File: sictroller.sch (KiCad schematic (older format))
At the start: 16 parts

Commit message: Hierarchical schematic
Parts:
- removed C? (x2): 1uF, symbol C_Small
- removed J?: TMDSCNCD28069, MODULE, symbol TMDSCNCD28069
- removed J?: CONN_02X13, symbol CONN_02X13
- removed J?: CONN_01X07, symbol CONN_01X07
- removed R? (x3): 10k, symbol R_Small
- removed R? (x6): 5k1, symbol R_Small
- removed R?: 10k, symbol R_ARRAY_8_10
- removed U?: 74LVC8T245, symbol 74LVC8T245
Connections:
- net labels removed: +15V, +3.3V, +5VD, FLT_DESAT, FLT_DESAT_LV, FLT_OTP, FLT_OTP_LV, GNDD, HV+, HV-, PHASE_A, PHASE_B, PHASE_C, PWM_AH, PWM_AL, PWM_BH, PWM_BL, PWM_CH, PWM_CL, PWR_RDY, PWR_RDY_LV, PWR_TEMP, ~PWR_RESET
- wire segments 103 -> 0
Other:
- note removed: "HV signals - use Micro-Fit, \nwatch creepage"

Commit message: V0 schematic complete (?)
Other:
- note added: "TODO (better):\nWelded contactor detection / protection\nLV from HV, LV batt charging?\nTemperature - motor, heatsink, power stage, air, batt?\nCrosslink to other string\nHuman interface\nContactor outputs (3 phases + bus + ?)\nADC precision reference\nCrystal oscillator\nGPS and air data interface"
- note added: "TODO (minimal):\nAux ADC and other signals on controlcard"
- note removed: "TODO (better):\nLV from HV, LV batt charging?\nTemperature - motor, heatsink, power stage, air, batt?\nCrosslink to other string\nHuman interface\nContactor outputs (3 phases + bus + ?)\nADC precision reference\nCrystal oscillator\nGPS and air data interface"
- note removed: "TODO (minimal):\n15V in, 5V and 3.3V reg\nPWM and faults to controlcard\nHV V and I monitoring inc filters\nPhase current (ext hall effect) inc filters\nPhase voltage inc filters\n(desired) bridge current via Vds inc filters"
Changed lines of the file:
@@
 LIBS:TMDSCNCD28069
 LIBS:74LVC8T245
+LIBS:MAX4195
 LIBS:sictroller-cache
 EELAYER 25 0
@@
 $EndDescr
 Text Notes 750  7900 0    60   ~ 0
-TODO (minimal):\n15V in, 5V and 3.3V reg\nPWM and faults to controlcard\nHV V and I monitoring inc filters\nPhase current (ext hall effect) inc filters\nPhase voltage inc filters\n(desired) bridge current via Vds inc filters
+TODO (minimal):\nAux ADC and other signals on controlcard
 Text Notes 3600 7900 0    60   ~ 0
-TODO (better):\nLV from HV, LV batt charging?\nTemperature - motor, heatsink, power stage, air, batt?\nCrosslink to other string\nHuman interface\nContactor outputs (3 phases + bus + ?)\nADC precision reference\nCrystal oscillator\nGPS and air data interface
+TODO (better):\nWelded contactor detection / protection\nLV from HV, LV batt charging?\nTemperature - motor, heatsink, power stage, air, batt?\nCrosslink to other string\nHuman interface\nContactor outputs (3 phases + bus + ?)\nADC precision reference\nCrystal oscillator\nGPS and air data interface
 $Sheet
-S 2650 1050 2350 3100
+S 4750 1500 2350 1850
 U 57A162B5
 F0 "Control Card" 60
 F1 "controlcard.sch" 60
+F2 "VFB_A" I L 4750 1900 60
+F3 "VFB_B" I L 4750 2000 60
+F4 "VFB_C" I L 4750 2100 60
+F5 "VFB_BUS" I L 4750 2200 60
+F6 "IFB_A" I L 4750 2350 60
+F7 "IFB_B" I L 4750 2450 60
+F8 "IFB_C" I L 4750 2550 60
+F9 "PWR_STG_TEMP" I L 4750 1650 60
+F10 "MOTOR_TEMP" I L 4750 1750 60
+F11 "IFB_BUS" I L 4750 2650 60
+F12 "Vds_A" I L 4750 2800 60
+F13 "Vds_B" I L 4750 2900 60
+F14 "Vds_C" I L 4750 3000 60
+F15 "PWM_AH" O R 7100 2350 60
+F16 "PWM_BH" O R 7100 2450 60
+F17 "PWM_CH" O R 7100 2550 60
+F18 "PWM_AL" O R 7100 2650 60
+F19 "PWM_BL" O R 7100 2750 60
+F20 "PWM_CL" O R 7100 2850 60
+F21 "~FLT_DESAT" I R 7100 1850 60
+F22 "~FLT_OTP" I R 7100 1950 60
+F23 "PWR_RDY" I R 7100 1650 60
+F24 "~PWR_RESET" O R 7100 2150 60
 $EndSheet
 $Sheet
-S 3000 4850 1900 1250
+S 4950 5000 1900 1250
 U 57A17AE7
 F0 "LV power supplies" 60
@@
 $EndSheet
 $Sheet
-S 6600 4550 1550 1250
+S 2500 1450 1350 1800
 U 57A17AFA
 F0 "Feedback" 60
 F1 "feedback.sch" 60
+F2 "VFB_A" O R 3850 1900 60
+F3 "VFB_B" O R 3850 2000 60
+F4 "VFB_C" O R 3850 2100 60
+F5 "IFB_A" O R 3850 2350 60
+F6 "IFB_B" O R 3850 2450 60
+F7 "IFB_C" O R 3850 2550 60
+F8 "VFB_BUS" O R 3850 2200 60
+F9 "PWR_TEMP" O R 3850 1650 60
+F10 "MOTOR_TEMP" O R 3850 1750 60
+F11 "IFB_BUS" O R 3850 2650 60
+F12 "Vds_A" O R 3850 2800 60
+F13 "Vds_B" O R 3850 2900 60
+F14 "Vds_C" O R 3850 3000 60
 $EndSheet
 $Sheet
-S 6500 1250 1150 1500
+S 7950 1500 1150 1500
 U 57A1662D
 F0 "Gate driver board" 60
 F1 "CGD15FB45P1.sch" 60
-F2 "PWR_RDY" O L 6500 1400 60
-F3 "FLT_DESAT" O L 6500 1600 60
-F4 "FLT_OTP" O L 6500 1700 60
-F5 "~PWR_RESET" I L 6500 1900 60
-F6 "PWM_AH" I L 6500 2100 60
-F7 "PWM_AL" I L 6500 2200 60
-F8 "PWM_BH" I L 6500 2300 60
-F9 "PWM_BL" I L 6500 2400 60
-F10 "PWM_CH" I L 6500 2500 60
-F11 "PWM_CL" I L 6500 2600 60
+F2 "PWR_RDY" O L 7950 1650 60
+F3 "~PWR_RESET" I L 7950 2150 60
+F4 "PWM_AH" I L 7950 2350 60
+F5 "PWM_AL" I L 7950 2450 60
+F6 "PWM_BH" I L 7950 2550 60
+F7 "PWM_BL" I L 7950 2650 60
+F8 "PWM_CH" I L 7950 2750 60
+F9 "PWM_CL" I L 7950 2850 60
+F10 "~FLT_DESAT" O L 7950 1850 60
+F11 "~FLT_OTP" O L 7950 1950 60
 $EndSheet
+Wire Wire Line
+	7100 2350 7950 2350
+Wire Wire Line
+	7950 2450 7100 2450
+Wire Wire Line
+	7100 2550 7950 2550
+Wire Wire Line
+	7950 2650 7100 2650
+Wire Wire Line
+	7100 2750 7950 2750
+Wire Wire Line
+	7950 2850 7100 2850
+Wire Wire Line
+	3850 1650 4750 1650
+Wire Wire Line
+	4750 1750 3850 1750
+Wire Wire Line
+	3850 1900 4750 1900
+Wire Wire Line
+	4750 2000 3850 2000
+Wire Wire Line
+	3850 2100 4750 2100
+Wire Wire Line
+	4750 2200 3850 2200
+Wire Wire Line
+	3850 2350 4750 2350
+Wire Wire Line
+	4750 2450 3850 2450
+Wire Wire Line
+	3850 2550 4750 2550
+Wire Wire Line
+	4750 2650 3850 2650
+Wire Wire Line
+	4750 2800 3850 2800
+Wire Wire Line
+	3850 2900 4750 2900
+Wire Wire Line
+	4750 3000 3850 3000
+Wire Wire Line
+	7950 2150 7100 2150
+Wire Wire Line
+	7100 1950 7950 1950
+Wire Wire Line
+	7950 1850 7100 1850
+Wire Wire Line
+	7100 1650 7950 1650
 $EndSCHEMATC

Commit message: Annotate, fix schematic DRC, footprint for DIMM100
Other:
- note added: "TODO (V2):\nWelded contactor detection / protection\nLV from HV, LV batt charging?\nTemperature - motor, heatsink, power stage, air, batt?\nCrosslink to other string\nHuman interface\nContactor outputs (3 phases + bus + ?)\nADC precision reference\nCrystal oscillator\nGPS and air data interface"
- note removed: "TODO (better):\nWelded contactor detection / protection\nLV from HV, LV batt charging?\nTemperature - motor, heatsink, power stage, air, batt?\nCrosslink to other string\nHuman interface\nContactor outputs (3 phases + bus + ?)\nADC precision reference\nCrystal oscillator\nGPS and air data interface"
- note removed: "TODO (minimal):\nAux ADC and other signals on controlcard"
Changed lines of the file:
@@
 Comment4 ""
 $EndDescr
-Text Notes 750  7900 0    60   ~ 0
-TODO (minimal):\nAux ADC and other signals on controlcard
 Text Notes 3600 7900 0    60   ~ 0
-TODO (better):\nWelded contactor detection / protection\nLV from HV, LV batt charging?\nTemperature - motor, heatsink, power stage, air, batt?\nCrosslink to other string\nHuman interface\nContactor outputs (3 phases + bus + ?)\nADC precision reference\nCrystal oscillator\nGPS and air data interface
+TODO (V2):\nWelded contactor detection / protection\nLV from HV, LV batt charging?\nTemperature - motor, heatsink, power stage, air, batt?\nCrosslink to other string\nHuman interface\nContactor outputs (3 phases + bus + ?)\nADC precision reference\nCrystal oscillator\nGPS and air data interface
 $Sheet
 S 4750 1500 2350 1850

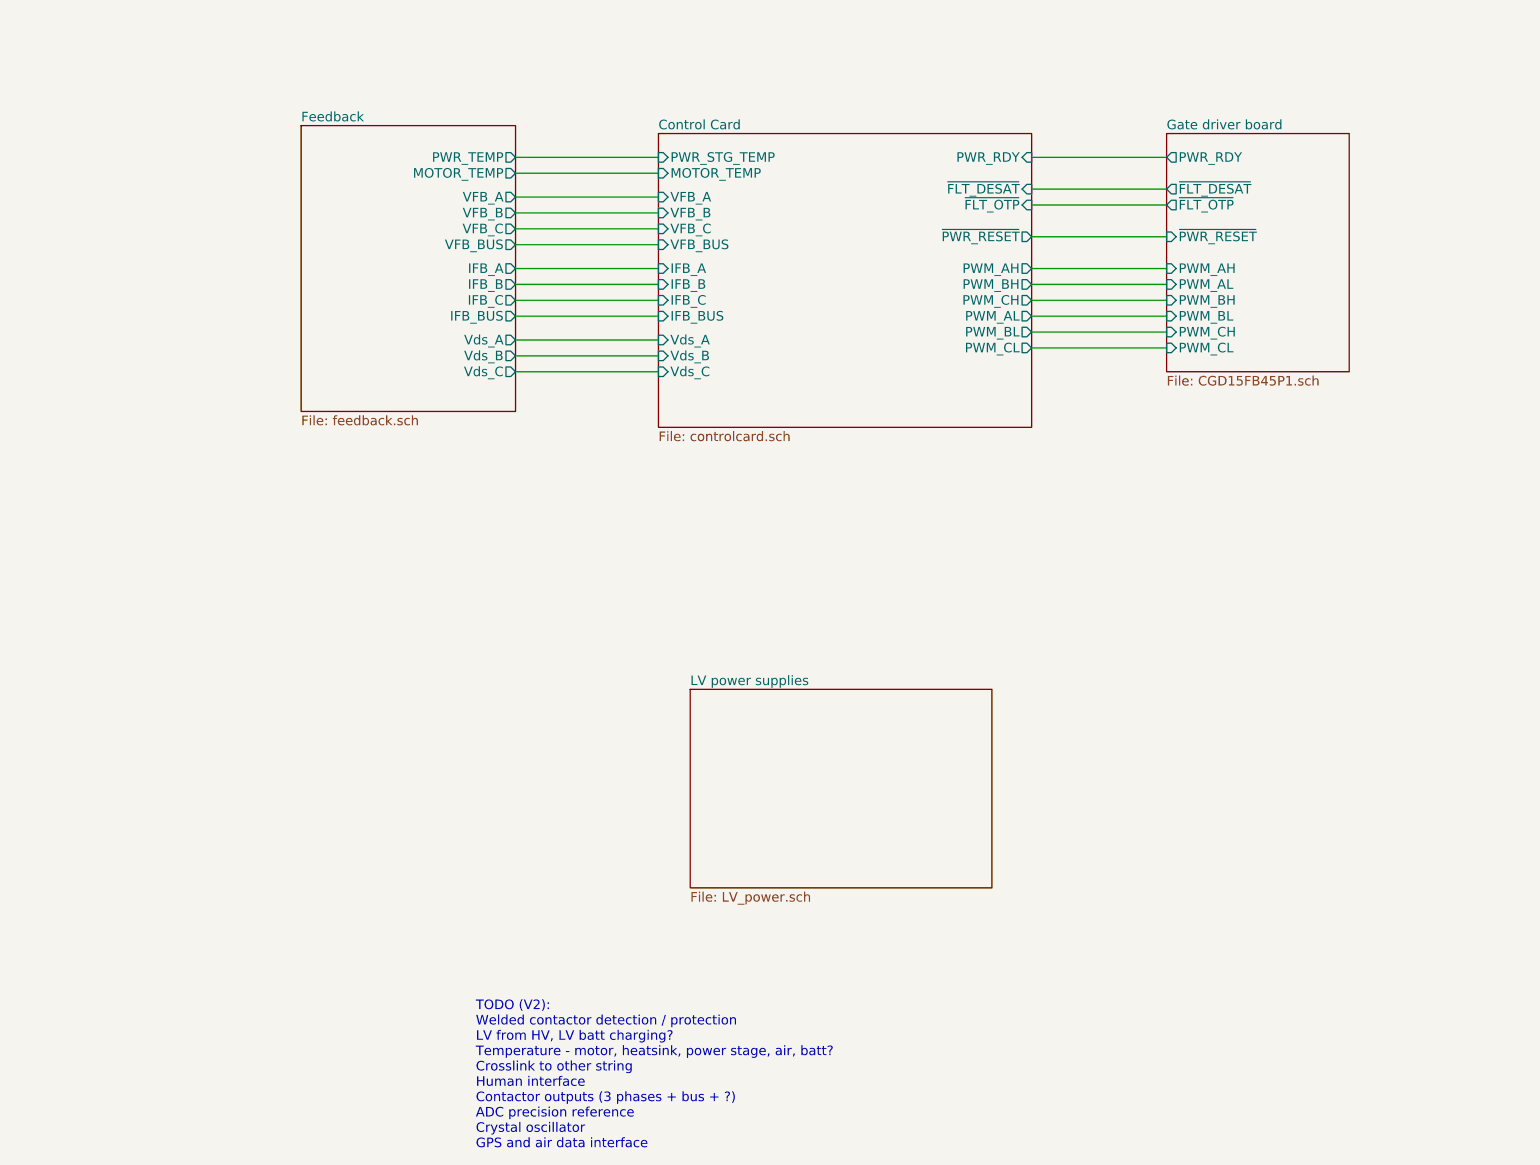
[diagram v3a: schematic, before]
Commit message: Add test points; PCB connectors placed
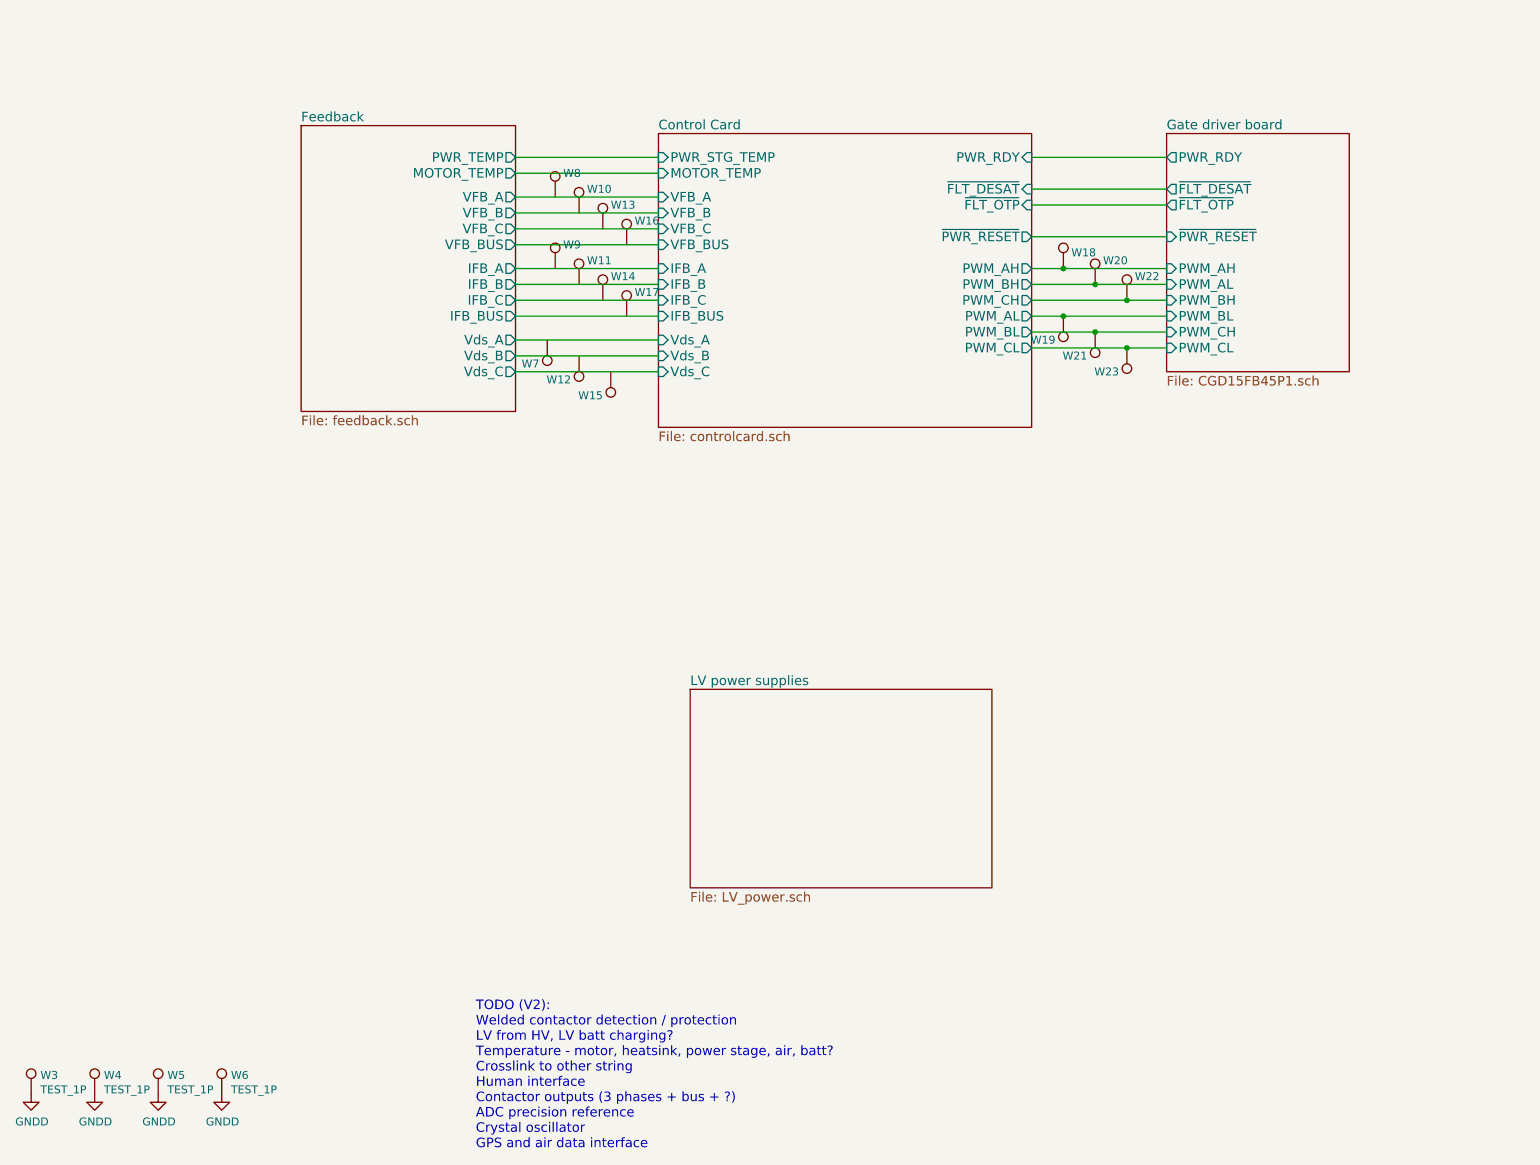
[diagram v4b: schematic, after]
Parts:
- added W10, W11, W12, W13, W14, W15, W16, W17, W18, W19, W20, W21, W22, W23, W3, W4, W5, W6, W7, W8, W9: TEST_1P, symbol TEST_1P
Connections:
- net Control Card/PWM_AH: now also W18.1
- net Control Card/PWM_AL: now also W19.1
- net Control Card/PWM_BH: now also W20.1
- net Control Card/PWM_BL: now also W21.1
- net Control Card/PWM_CH: now also W22.1
- net Control Card/PWM_CL: now also W23.1
- new net GNDD: W3.1, W4.1, W5.1, W6.1
